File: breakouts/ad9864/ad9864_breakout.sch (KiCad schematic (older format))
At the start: 30 parts

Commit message: work on ad9864 schematic, vco and if
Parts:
- removed C?: 10 nF, symbol C_Small
- removed D?: D_Small, symbol D_Small
- added C? (x2): 100 nF, symbol C_Small
- added C? (x4): DNP, symbol C_Small
- added C? (x2): 10 uF, symbol C_Small
- added C?: 330 pF, symbol C_Small
- added C? (x3): 10 nF, symbol C_Small
- added C?: 1 nF, symbol C_Small
- added C? (x3): TBD, symbol C_Small
- added D?: LED, symbol LED
- added D?: 1SV288, symbol D_Schottky_x2_KCom_AAK
- added F?: F_Small, symbol F_Small
- added L?: L_Small, symbol L_Small
- added L?: 1.2 uH, symbol L_Small
- added L?: 10 mH, symbol L_Small
- added P?: CONN_01X02, symbol CONN_01X02
- added R? (x6): 0, symbol R_Small
- added R? (x2): 1k, symbol R_Small
- added R? (x5): DNP, symbol R_Small
- added R?: 51, symbol R_Small
- added R?: 28.7k, symbol R_Small
- added R?: 10k, symbol R_Small
- added R?: 2.87k, symbol R_Small
- added R?: TBD, symbol R_Small
- added R?: 57.6, symbol R_Small
- added RP? (x2): 22, symbol R_PACK4
- added U?: TXCO, symbol TXCO
- added U? (x4): CONN_SMA, symbol CONN_SMA
- added U?: max2605, symbol max2605
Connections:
- net +3V3: now also C?.1, C?.1, C?.1, C?.2, D?.2 (A), F?.1, L?.1, R?.1, R?.1, U?.4 (VCC), U?.5 (Vcc); no longer C?.1, C?.1, U?.26 (VDDD), U?.27 (VDDH)
- net CLKN: now also R?.2
- net CLKP: now also C?.2, R?.2
- net GND: now also C?.2, C?.1, C?.1, C?.2, C?.2, C?.2, C?.2, C?.2, C?.2, C?.2, C?.2, D?.1 (A), D?.2 (A), L?.1, P?.2 (P2), R?.1, R?.2, R?.2, R?.2, R?.2, U?.2 (GND), U?.2 (GND), U?.2 (GND), U?.2 (GND), U?.2 (GND), U?.2 (GND), U?.3 (GND), U?.3 (GND), U?.3 (GND), U?.3 (GND), U?.4 (GND), U?.4 (GND), U?.4 (GND), U?.4 (GND), U?.5 (GND), U?.5 (GND), U?.5 (GND), U?.5 (GND)
- net IFIN: now also C?.2
- net IOUTC: now also C?.1, R?.1, R?.2
- net LON: now also R?.1, R?.2
- net LOP: now also C?.1, R?.2
- net PE: now also RP?.7 (R2); no longer U?.25 (PE)
- net at U?.23 (PC): now also RP?.4 (P4)
- net at U?.24 (PD): now also RP?.3 (P3)
- net at U?.35 (FREF): now also C?.1, C?.1, R?.2
- net IOUTL: now reaches U?.38 (IOUTL)
- net IOUTL: now also C?.1, R?.1, R?.1
- net at C?.2: now also R?.1
- net CLKOUT: no longer names the net of U?.28 (CLKOUT)
- net CLKOUT: now also RP?.1 (P1)
- net DOUTA: no longer names the net of U?.29 (DOUTA)
- net DOUTA: now also RP?.4 (P4)
- net DOUTB: no longer names the net of U?.30 (DOUTB)
- net DOUTB: now also RP?.3 (P3)
- net FS: no longer names the net of U?.31 (FS)
- net FS: now also R?.1, RP?.2 (P2)
- net SYNCB: no longer names the net of U?.33 (SYNCB)
- net SYNCB: now also R?.2, R?.2, RP?.1 (P1)
- new net: RP?.2 (P2), U?.25 (PE)
- new net: C?.1, U?.26 (VDDD)
- new net: C?.1, C?.1, L?.2, U?.27 (VDDH)
- new net: R?.1, U?.3 (OSC)
- new net: C?.2, U?.1 (RF) (x2)
- new net: F?.2, P?.1 (P1)
- new net: D?.1 (K), R?.1
- new net: R?.1, R?.2, U?.1 (RF) (x2)
- new net: C?.2, C?.2, D?.3 (K), R?.1
- new net: C?.1, R?.2 (x2)
- new net: C?.1, C?.1, L?.1, R?.1
- new net: L?.2, R?.1, R?.2
- new net: L?.2, U?.1 (IND)
- new net: C?.2, R?.2, U?.3 (TUNE)
- new net: R?.1, U?.4 (OUT-)
- new net: R?.1, U?.6 (OUT+)
- new net: C?.1, R?.1, R?.2
- new net ADC_CLKOUT: RP?.8 (R1)
- new net ADC_DOUTA: RP?.5 (R4)
- new net ADC_DOUTB: RP?.6 (R3)
- new net ADC_FS: RP?.7 (R2)
- new net ADC_SYNCB: RP?.8 (R1)
- new net FREF_XCO_EN: U?.1 (EN)
- new net PC: RP?.5 (R4)
- new net PD: RP?.6 (R3)
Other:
- moved on the sheet: C?

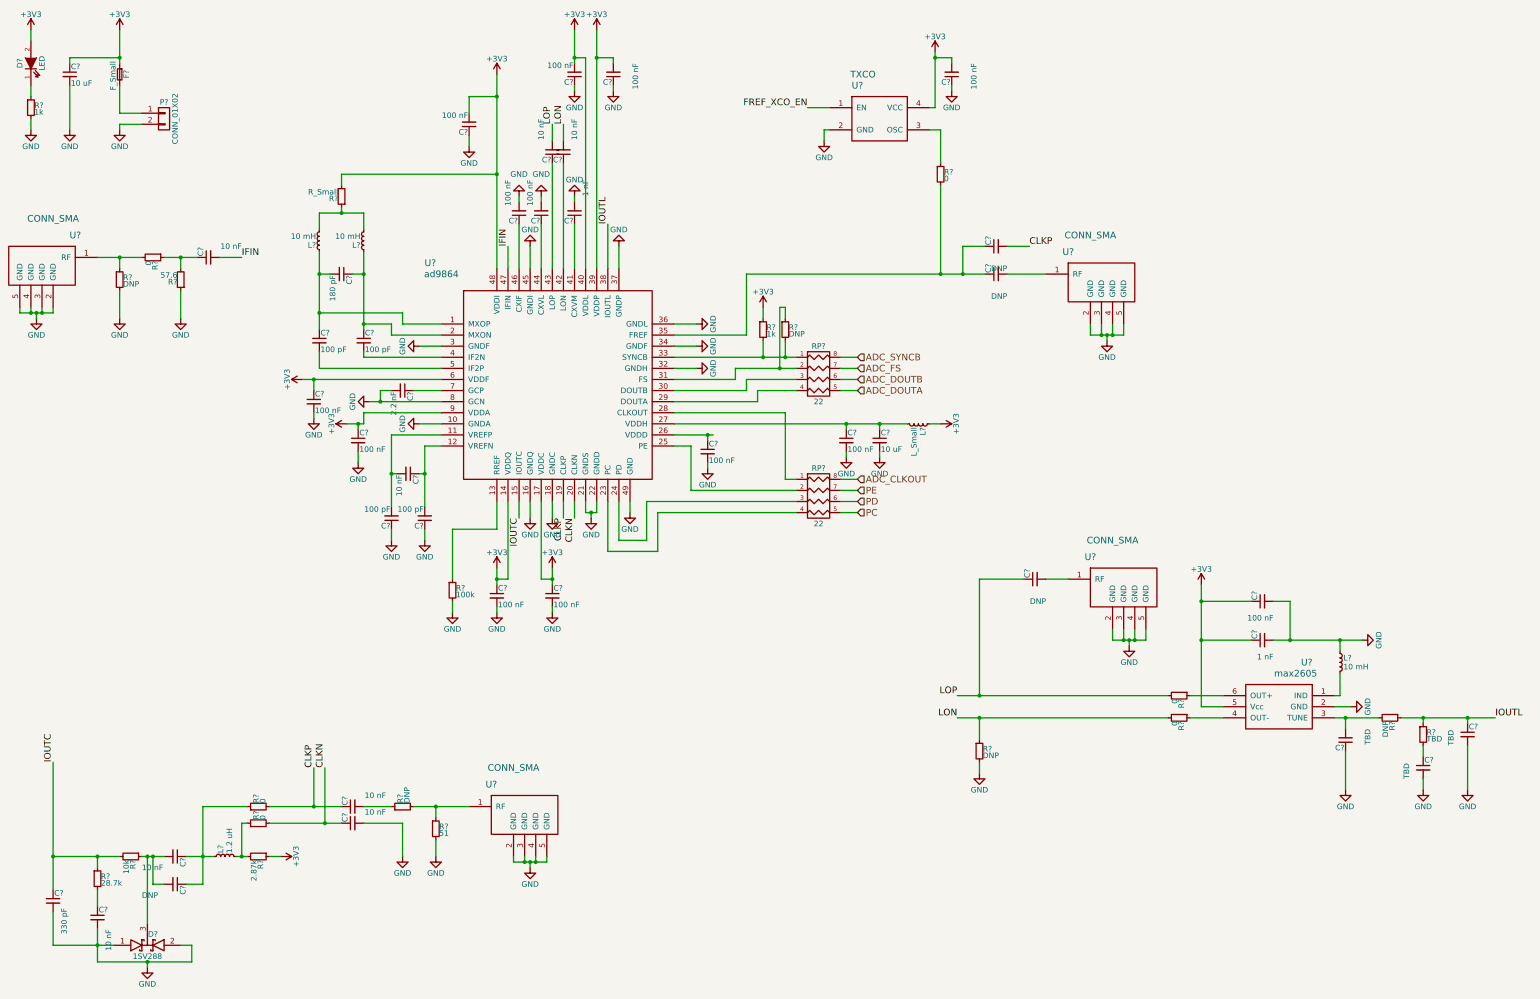
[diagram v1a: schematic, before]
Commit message: finished schematic and footprint assignment
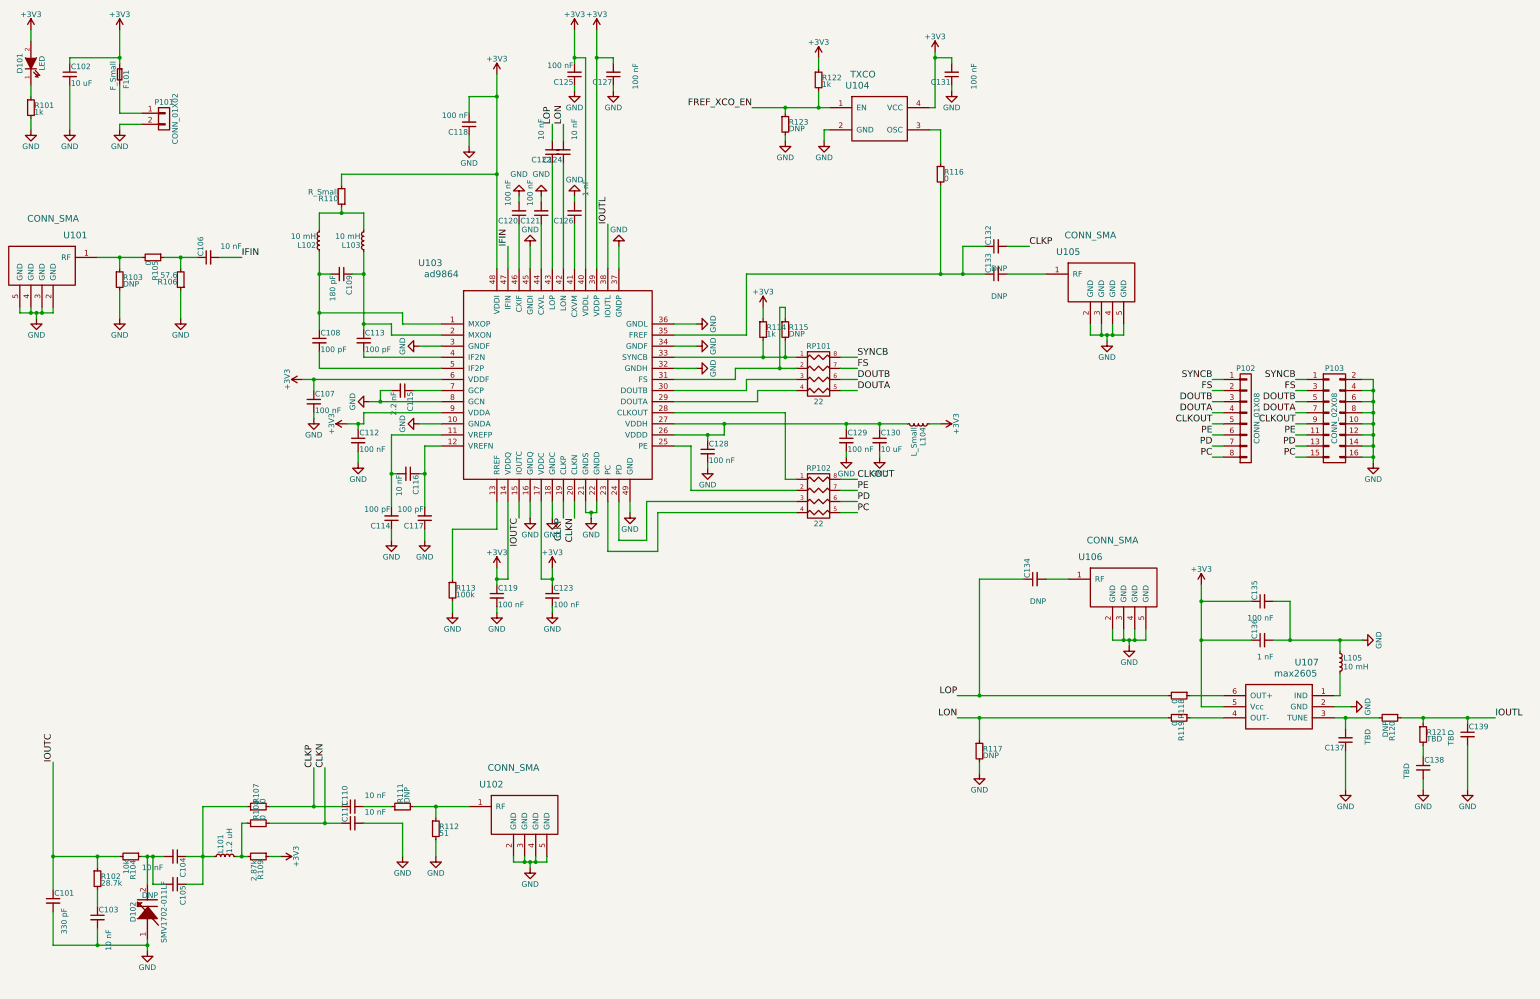
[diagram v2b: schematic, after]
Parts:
- removed D?: 1SV288, symbol D_Schottky_x2_KCom_AAK
- added D102: SMV1702-011LF, Diodes_SMD:SOD-323, symbol VARICAP
- added P102: CONN_01X08, Pin_Headers:Pin_Header_Straight_1x08, symbol CONN_01X08
- added P103: CONN_02X08, Pin_Headers:Pin_Header_Straight_2x08, symbol CONN_02X08
- added R122: 1k, Resistors_SMD:R_0603, symbol R_Small
- added R123: DNP, Resistors_SMD:R_0603, symbol R_Small
- C101, C103, C104, C105, C106, C107, C108, C109, C110, C111, C112, C113, C114, C115, C116, C117, C118, C119, C120, C121, C122, C123, C124, C125, C126, C127, C128, C129, C131, C132, C133, C134, C135, C136, C137, C138, C139: renamed from C?; footprint (none) -> Capacitors_SMD:C_0603
- C102, C130: renamed from C?; footprint (none) -> Capacitors_SMD:C_0805
- D101: renamed from D?; footprint (none) -> LEDs:LED_0603
- F101: renamed from F?; footprint (none) -> Resistors_SMD:R_1812
- L101, L102, L103, L105: renamed from L?; footprint (none) -> Resistors_SMD:R_0805
- L104: renamed from L?; footprint (none) -> Resistors_SMD:R_0603
- P101: renamed from P?; footprint (none) -> Terminal_Blocks:TerminalBlock_Pheonix_PT-3.5mm_2pol
- R101, R102, R103, R104, R105, R106, R107, R108, R109, R110, R111, R112, R113, R114, R115, R116, R117, R118, R119, R120, R121: renamed from R?; footprint (none) -> Resistors_SMD:R_0603
- RP101, RP102: renamed from RP?; footprint (none) -> Resistors_SMD:R_Array_Concave_4x0603
- U101, U102, U105, U106: renamed from U?; footprint (none) -> vna_footprints:732512200_SMA
- U103: renamed from U?; footprint (none) -> Housings_DFN_QFN:QFN-48-1EP_7x7mm_Pitch0.5mm
- U104: renamed from U?; footprint (none) -> vna_footprints:crystal_FA238-TSX3225
- U107: renamed from U?; footprint (none) -> TO_SOT_Packages_SMD:SOT-23-6
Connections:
- net +3V3: now also R122.1
- net FREF_XCO_EN: now also R122.2, R123.1
- net GND: now also D102.1 (ANODE), P103.10 (P10), P103.12 (P12), P103.14 (P14), P103.16 (P16), P103.2 (P2), P103.4 (P4), P103.6 (P6), P103.8 (P8), R123.2
- net PC: now also P102.8 (P8), P103.15 (P15)
- net PD: now also P102.7 (P7), P103.13 (P13)
- net PE: now also P102.6 (P6), P103.11 (P11)
- net at C128.1, U103.26 (VDDD): now also C129.1, C130.1, L104.2, U103.27 (VDDH)
- net at C104.2, C105.2, R104.1: now also D102.2 (CATHODE)
- net ADC_CLKOUT renamed CLKOUT
- net CLKOUT: now also P102.5 (P5), P103.9 (P9)
- net ADC_DOUTA renamed DOUTA
- net DOUTA: now also P102.4 (P4), P103.7 (P7)
- net ADC_DOUTB renamed DOUTB
- net DOUTB: now also P102.3 (P3), P103.5 (P5)
- net ADC_FS renamed FS
- net FS: now also P102.2 (P2), P103.3 (P3)
- net ADC_SYNCB renamed SYNCB
- net SYNCB: now also P102.1 (P1), P103.1 (P1)

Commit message: component placement on ad9864 breakout
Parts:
- L102, L103, L105: value 10 mH -> 10 uH
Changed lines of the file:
@@
 P 3850 2800
 F 0 "L103" H 3880 2840 50  0000 L CNN
-F 1 "10 mH" H 3880 2760 50  0000 L CNN
+F 1 "10 uH" H 3880 2760 50  0000 L CNN
 F 2 "Resistors_SMD:R_0805" H 3850 2800 50  0001 C CNN
 F 3 "" H 3850 2800 50  0000 C CNN
@@
 P 3450 2800
 F 0 "L102" H 3480 2840 50  0000 L CNN
-F 1 "10 mH" H 3480 2760 50  0000 L CNN
+F 1 "10 uH" H 3480 2760 50  0000 L CNN
 F 2 "Resistors_SMD:R_0805" H 3450 2800 50  0001 C CNN
 F 3 "" H 3450 2800 50  0000 C CNN
@@
 P 12650 6600
 F 0 "L105" H 12680 6640 50  0000 L CNN
-F 1 "10 mH" H 12680 6560 50  0000 L CNN
+F 1 "10 uH" H 12680 6560 50  0000 L CNN
 F 2 "Resistors_SMD:R_0805" H 12650 6600 50  0001 C CNN
 F 3 "" H 12650 6600 50  0000 C CNN

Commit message: finished ad9864 silkscreen cleanup, ordered r0
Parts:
- added U?: mounting_box, symbol mounting_box
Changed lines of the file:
@@
 	7650 1650 7650 1600
 Connection ~ 7650 1600
+$Comp
+L mounting_box U?
+U 1 1 57CA7A8F
+P 12750 2300
+F 0 "U?" H 12750 2300 60  0000 C CNN
+F 1 "mounting_box" H 12700 2450 60  0000 C CNN
+F 2 "" H 12750 2300 60  0000 C CNN
+F 3 "" H 12750 2300 60  0000 C CNN
+	1    12750 2300
+	1    0    0    -1
+$EndComp
 $EndSCHEMATC

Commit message: tested ethernet vna control
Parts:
- U108: renamed from U?; footprint (none) -> vna_footprints:momo
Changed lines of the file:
@@
 Connection ~ 7650 1600
 $Comp
-L mounting_box U?
+L mounting_box U108
 U 1 1 57CA7A8F
 P 12750 2300
-F 0 "U?" H 12750 2300 60  0000 C CNN
+F 0 "U108" H 12750 2300 60  0000 C CNN
 F 1 "mounting_box" H 12700 2450 60  0000 C CNN
-F 2 "" H 12750 2300 60  0000 C CNN
+F 2 "vna_footprints:momo" H 12750 2300 60  0001 C CNN
 F 3 "" H 12750 2300 60  0000 C CNN
 	1    12750 2300
